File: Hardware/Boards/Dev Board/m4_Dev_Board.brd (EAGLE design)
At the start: 50.2 x 53.6 mm, 19 parts, among them J1 POWER_JACKPTH, U1 MK10DN512ZVLL10

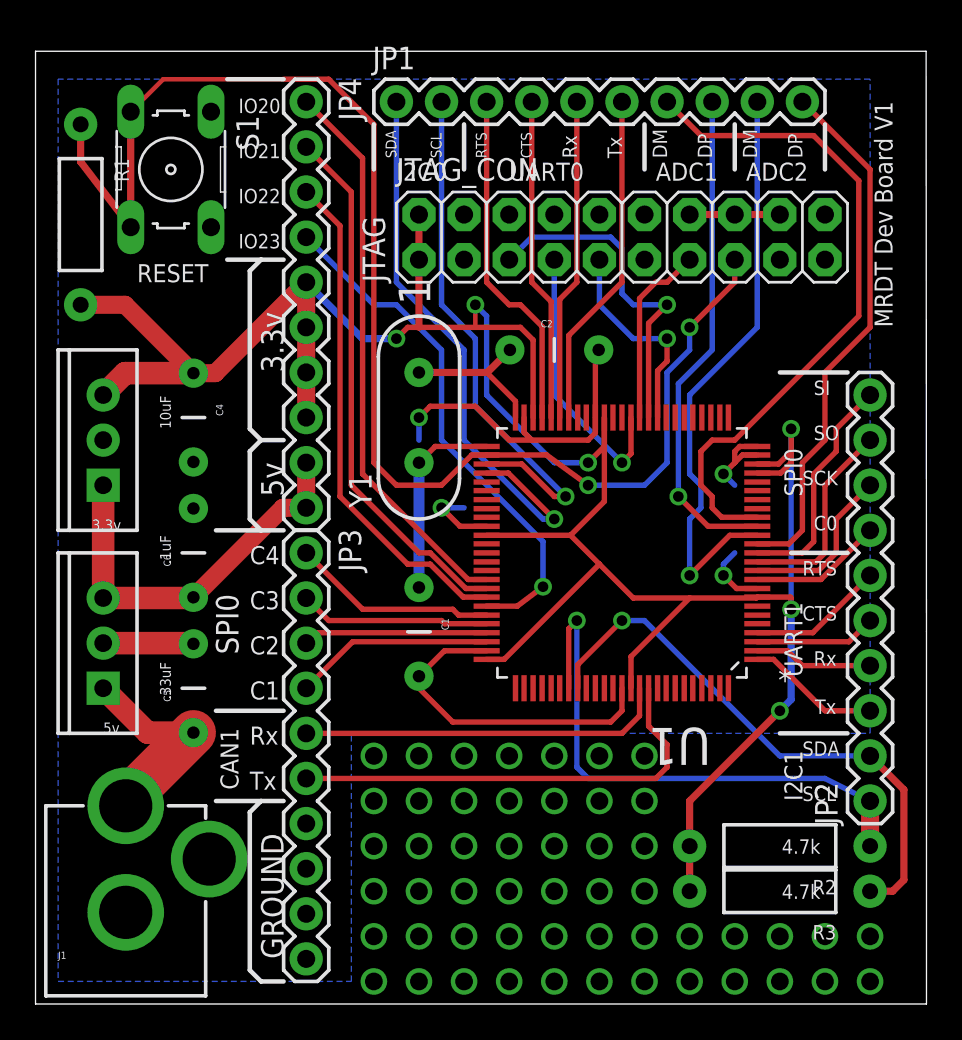
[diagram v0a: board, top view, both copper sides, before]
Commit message: Updated DRC, fixed some of the clearance issues. Still need to fix other clearance issues, remove vias from underneath the crystal.
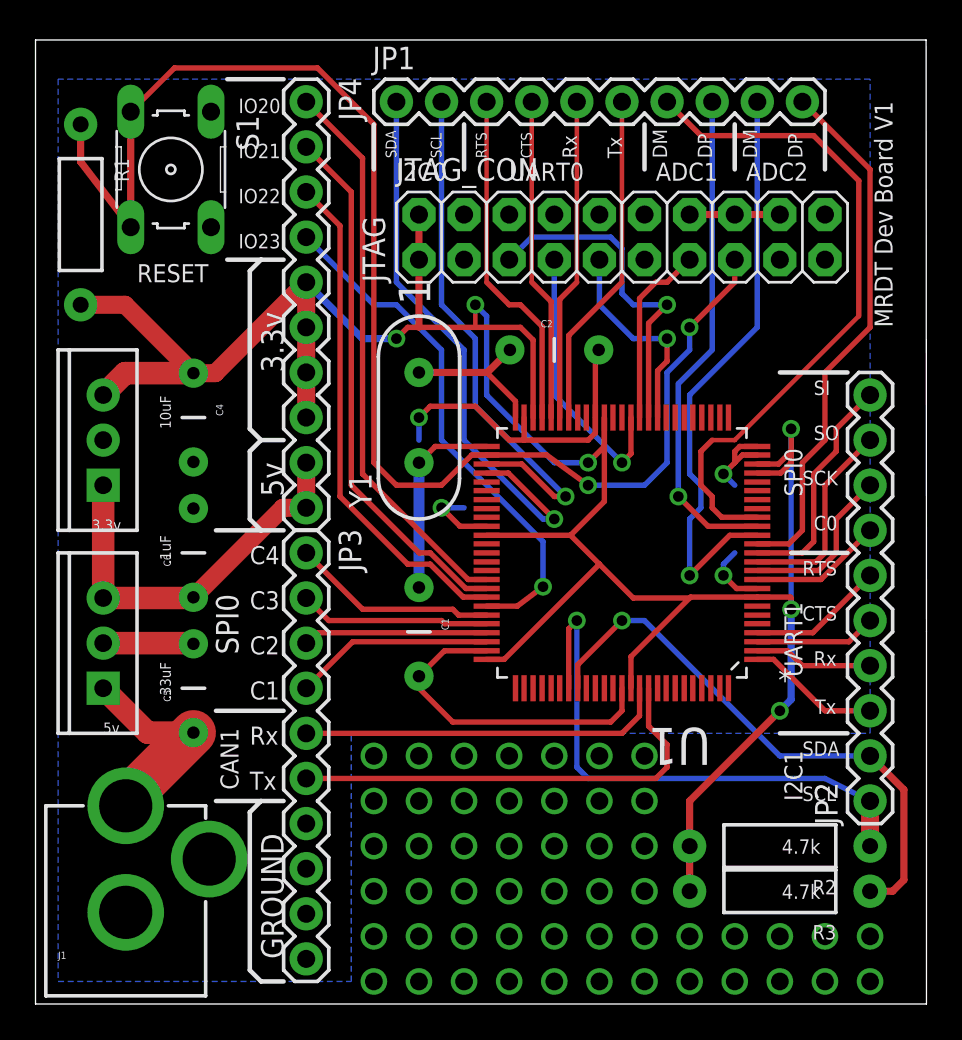
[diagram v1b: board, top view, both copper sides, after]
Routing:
- net RESET: track 79.6 -> 80.2 mm
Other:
- board size 50.2 x 53.6 mm -> 50.2 x 54.3 mm
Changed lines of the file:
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@@
 <wire x1="0" y1="-1.27" x2="50.165" y2="-1.27" width="0" layer="20"/>
 <wire x1="50.165" y1="-1.27" x2="50.165" y2="19.685" width="0" layer="20"/>
-<wire x1="50.165" y1="19.685" x2="50.145" y2="52.375" width="0" layer="20"/>
-<wire x1="50.145" y1="52.375" x2="0" y2="52.375" width="0" layer="20"/>
-<wire x1="0" y1="52.375" x2="0" y2="-1.27" width="0" layer="20"/>
+<wire x1="50.165" y1="19.685" x2="50.145" y2="53.01" width="0" layer="20"/>
+<wire x1="50.145" y1="53.01" x2="0" y2="53.01" width="0" layer="20"/>
+<wire x1="0" y1="53.01" x2="0" y2="-1.27" width="0" layer="20"/>
 <text x="13.97" y="1.27" size="1.27" layer="121" rot="R90">GROUND</text>
 <wire x1="13.97" y1="10.16" x2="12.7" y2="10.16" width="0.254" layer="121"/>
@@
 <param name="mdSmdPad" value="8mil"/>
 <param name="mdSmdVia" value="8mil"/>
-<param name="mdSmdSmd" value="8mil"/>
+<param name="mdSmdSmd" value="6mil"/>
 <param name="mdViaViaSameLayer" value="8mil"/>
 <param name="mnLayersViaInSmd" value="2"/>
@@
 <wire x1="38.735" y1="22.86" x2="38.735" y2="23.495" width="0.3048" layer="16"/>
 <wire x1="38.735" y1="23.495" x2="39.37" y2="24.13" width="0.3048" layer="16"/>
-<wire x1="27.5082" y1="31.75" x2="27.5082" y2="30.9118" width="0.3048" layer="1"/>
-<wire x1="27.5082" y1="30.9118" x2="27.94" y2="30.48" width="0.3048" layer="1"/>
+<wire x1="27.5082" y1="31.75" x2="27.5082" y2="30.48" width="0.3048" layer="1"/>
+<wire x1="26.67" y1="30.48" x2="27.5082" y2="30.48" width="0.3048" layer="1"/>
 <wire x1="27.94" y1="30.48" x2="31.115" y2="30.48" width="0.3048" layer="1"/>
 <wire x1="31.5214" y1="31.75" x2="31.5214" y2="30.8864" width="0.3048" layer="1"/>
@@
 <via x="22.86" y="26.67" extent="1-16" drill="0.6" shape="square"/>
 <wire x1="22.86" y1="26.67" x2="24.13" y2="26.67" width="0.3048" layer="16"/>
-<wire x1="27.94" y1="30.48" x2="26.67" y2="30.48" width="0.3048" layer="1"/>
 <wire x1="26.67" y1="30.48" x2="24.765" y2="32.385" width="0.3048" layer="1"/>
 <wire x1="24.765" y1="32.385" x2="22.225" y2="32.385" width="0.3048" layer="1"/>
@@
 <via x="21.59" y="31.75" extent="1-16" drill="0.6" shape="square"/>
 <wire x1="21.59" y1="31.75" x2="21.59" y2="30.48" width="0.3048" layer="16"/>
+<wire x1="27.5082" y1="30.48" x2="27.94" y2="30.48" width="0.3048" layer="1"/>
 </signal>
 <signal name="+3V3">
@@
 <wire x1="15.24" y1="36.83" x2="15.24" y2="34.29" width="1.016" layer="1"/>
 <wire x1="15.24" y1="34.29" x2="15.24" y2="31.75" width="1.016" layer="1"/>
-<wire x1="40.64" y1="21.6408" x2="40.5892" y2="21.59" width="0.3048" layer="1"/>
-<wire x1="40.5892" y1="21.59" x2="36.83" y2="21.59" width="0.3048" layer="1"/>
 <wire x1="36.83" y1="21.59" x2="33.528" y2="18.288" width="0.3048" layer="1"/>
 <wire x1="33.528" y1="18.288" x2="33.528" y2="16.51" width="0.3048" layer="1"/>
@@
 <wire x1="41.91" y1="15.24" x2="42.545" y2="15.875" width="0.4064" layer="16"/>
 <wire x1="42.545" y1="15.875" x2="42.545" y2="20.955" width="0.4064" layer="16"/>
+<wire x1="40.64" y1="21.6408" x2="36.8808" y2="21.6408" width="0.3048" layer="1"/>
+<wire x1="36.8808" y1="21.6408" x2="36.83" y2="21.59" width="0.3048" layer="1"/>
 </signal>
 <signal name="RESET">
@@
 <wire x1="20.32" y1="27.94" x2="19.05" y2="29.21" width="0.3048" layer="1"/>
 <wire x1="19.05" y1="29.21" x2="19.05" y2="48.26" width="0.3048" layer="1"/>
-<wire x1="19.05" y1="48.26" x2="16.51" y2="50.8" width="0.3048" layer="1"/>
-<wire x1="16.51" y1="50.8" x2="13.97" y2="50.8" width="0.3048" layer="1"/>
+<wire x1="19.05" y1="48.26" x2="15.875" y2="51.435" width="0.3048" layer="1"/>
 <wire x1="5.3594" y1="42.4688" x2="5.3594" y2="48.9712" width="0.4064" layer="1"/>
 <wire x1="25.4" y1="29.6418" x2="28.7782" y2="29.6418" width="0.3048" layer="1"/>
 <wire x1="28.7782" y1="29.6418" x2="31.115" y2="27.94" width="0.3048" layer="1"/>
-<wire x1="13.97" y1="50.8" x2="7.1882" y2="50.8" width="0.254" layer="1"/>
-<wire x1="5.3594" y1="48.9712" x2="7.1882" y2="50.8" width="0.254" layer="1"/>
+<wire x1="15.875" y1="51.435" x2="7.8232" y2="51.435" width="0.3048" layer="1"/>
+<wire x1="7.8232" y1="51.435" x2="5.3594" y2="48.9712" width="0.3048" layer="1"/>
 </signal>
 <signal name="V+">
@@
 <wire x1="37.465" y1="27.94" x2="37.465" y2="29.845" width="0.3048" layer="1"/>
 <wire x1="37.465" y1="29.845" x2="38.1" y2="30.48" width="0.3048" layer="1"/>
-<wire x1="38.1" y1="30.48" x2="39.37" y2="30.48" width="0.3048" layer="1"/>
-<wire x1="39.37" y1="30.48" x2="46.355" y2="37.465" width="0.3048" layer="1"/>
+<wire x1="38.1" y1="30.48" x2="39.37" y2="30.48" width="0.254" layer="1"/>
+<wire x1="39.37" y1="30.48" x2="46.355" y2="37.465" width="0.254" layer="1"/>
 </signal>
 <signal name="DAC0_OUT">
@@
 <wire x1="30.0228" y1="31.75" x2="30.0228" y2="36.3728" width="0.3048" layer="1"/>
 <wire x1="30.0228" y1="36.3728" x2="33.02" y2="39.37" width="0.3048" layer="1"/>
-<wire x1="33.02" y1="39.37" x2="33.02" y2="49.53" width="0.3048" layer="1"/>
+<wire x1="33.02" y1="39.37" x2="33.02" y2="49.53" width="0.254" layer="1"/>
 </signal>
 <signal name="UART0_RX">
@@
 <wire x1="29.5148" y1="31.75" x2="29.5148" y2="38.4048" width="0.3048" layer="1"/>
 <wire x1="29.5148" y1="38.4048" x2="30.48" y2="39.37" width="0.3048" layer="1"/>
-<wire x1="30.48" y1="39.37" x2="30.48" y2="49.53" width="0.3048" layer="1"/>
+<wire x1="30.48" y1="39.37" x2="30.48" y2="49.53" width="0.254" layer="1"/>
 </signal>
 <signal name="UART0_CTS">
@@
 <wire x1="29.0322" y1="31.75" x2="29.0322" y2="38.2778" width="0.3048" layer="1"/>
 <wire x1="29.0322" y1="38.2778" x2="27.94" y2="39.37" width="0.3048" layer="1"/>
-<wire x1="27.94" y1="39.37" x2="27.94" y2="49.53" width="0.3048" layer="1"/>
+<wire x1="27.94" y1="39.37" x2="27.94" y2="49.53" width="0.254" layer="1"/>
 </signal>
 <signal name="UART0_RTS">
@@
 <wire x1="27.305" y1="38.1" x2="26.67" y2="38.1" width="0.3048" layer="1"/>
 <wire x1="26.67" y1="38.1" x2="25.4" y2="39.37" width="0.3048" layer="1"/>
-<wire x1="25.4" y1="39.37" x2="25.4" y2="49.53" width="0.3048" layer="1"/>
+<wire x1="25.4" y1="39.37" x2="25.4" y2="49.53" width="0.254" layer="1"/>
 </signal>
 <signal name="GPIO20">
@@
 </signal>
 </signals>
+<errors>
+</errors>
 </board>
 </drawing>

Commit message: Fixed clearance issues
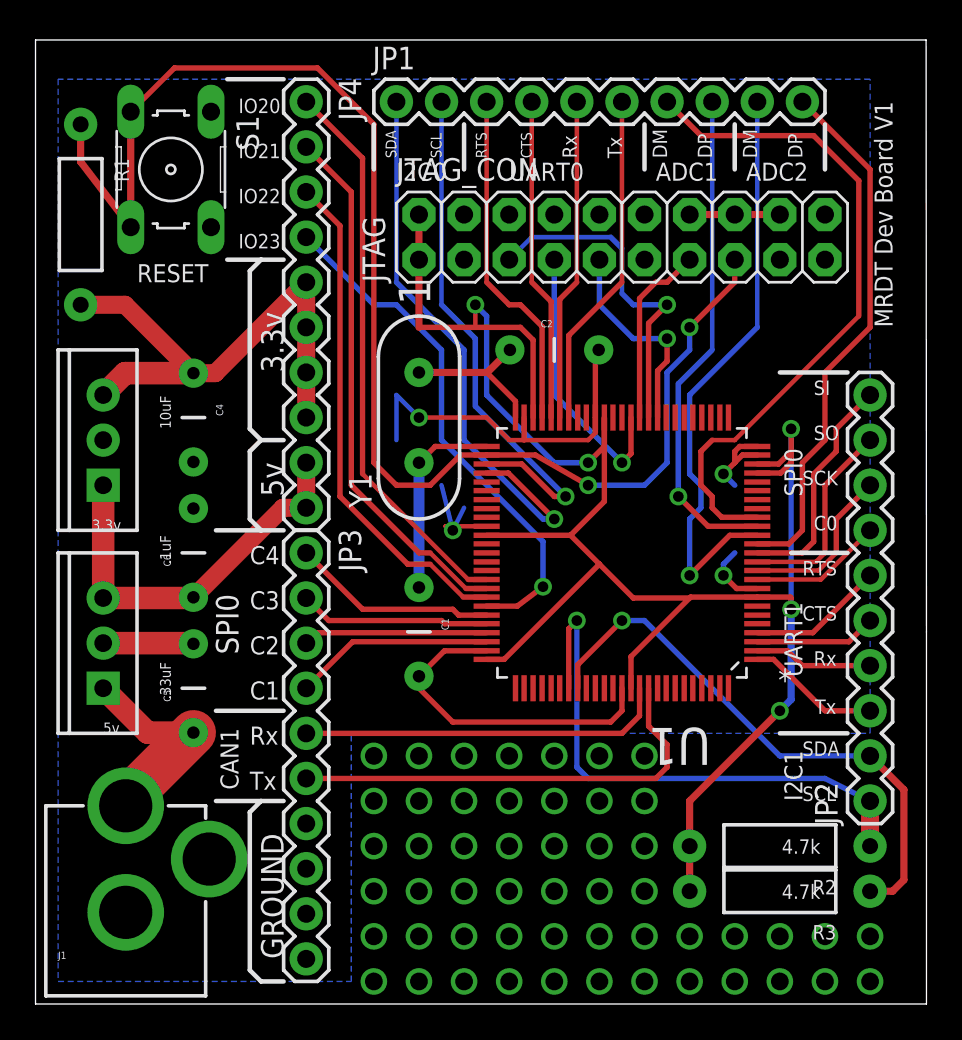
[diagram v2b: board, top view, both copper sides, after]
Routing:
- net +3V3: track 148.2 -> 140.3 mm, vias 6 -> 5
- net GND: track 60.7 -> 65.8 mm
